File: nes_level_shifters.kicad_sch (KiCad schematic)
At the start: 17 parts, among them J2 NES 3v3 TP, U1 74ALVC164245, U2 74ALVC164245, U3 74ALVC164245, U4 74ALVC164245

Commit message: Create project-local libraries
Signed-off-by: Chris Frantz <frantzcj@gmail.com>
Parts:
- C10, C11, C12, C13, C14, C7, C8, C9: symbol Device:C -> Library:C
- J2: symbol Connector_Generic:Conn_02x36_Odd_Even -> Library:Conn_02x36_Odd_Even
- R43, R44, R45, R46: symbol Device:R -> Library:R
- U1, U2, U3, U4: symbol 74xx:74ALVC164245 -> Library:74ALVC164245
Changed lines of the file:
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@@
 	)
 	(symbol
-		(lib_id "Device:C")
+		(lib_id "Library:C")
 		(at 118.11 26.67 90)
 		(unit 1)
@@
 	)
 	(symbol
-		(lib_id "power:VCC")
+		(lib_id "Library:VCC")
 		(at 157.48 33.02 0)
 		(unit 1)
@@
 	)
 	(symbol
-		(lib_id "74xx:74ALVC164245")
+		(lib_id "Library:74ALVC164245")
 		(at 132.08 60.96 0)
 		(unit 1)
@@
 	)
 	(symbol
-		(lib_id "power:GND")
+		(lib_id "Library:GND")
 		(at 59.69 190.5 0)
 		(unit 1)
@@
 	)
 	(symbol
-		(lib_id "74xx:74ALVC164245")
+		(lib_id "Library:74ALVC164245")
 		(at 55.88 60.96 0)
 		(unit 1)
@@
 	)
 	(symbol
-		(lib_id "power:GND")
+		(lib_id "Library:GND")
 		(at 114.3 26.67 0)
 		(unit 1)
@@
 	)
 	(symbol
-		(lib_id "power:GND")
+		(lib_id "Library:GND")
 		(at 118.11 123.19 0)
 		(unit 1)
@@
 	)
 	(symbol
-		(lib_id "power:VCC")
+		(lib_id "Library:VCC")
 		(at 96.52 35.56 0)
 		(unit 1)
@@
 	)
 	(symbol
-		(lib_id "power:VCC")
+		(lib_id "Library:VCC")
 		(at 45.72 26.67 0)
 		(unit 1)
@@
 	)
 	(symbol
-		(lib_id "Device:R")
+		(lib_id "Library:R")
 		(at 96.52 39.37 0)
 		(unit 1)
@@
 	)
 	(symbol
-		(lib_id "Device:R")
+		(lib_id "Library:R")
 		(at 157.48 36.83 0)
 		(unit 1)
@@
 	)
 	(symbol
-		(lib_id "power:GND")
+		(lib_id "Library:GND")
 		(at 146.05 123.19 0)
 		(unit 1)
@@
 	)
 	(symbol
-		(lib_id "power:VCC")
+		(lib_id "Library:VCC")
 		(at 62.23 121.92 0)
 		(unit 1)
@@
 	)
 	(symbol
-		(lib_id "power:GND")
+		(lib_id "Library:GND")
 		(at 66.04 26.67 0)
 		(unit 1)
@@
 	)
 	(symbol
-		(lib_id "power:VCC")
+		(lib_id "Library:VCC")
 		(at 125.73 123.19 0)
 		(unit 1)
@@
 	)
 	(symbol
-		(lib_id "power:GND")
+		(lib_id "Library:GND")
 		(at 142.24 26.67 0)
 		(unit 1)
@@
 	)
 	(symbol
-		(lib_id "power:GND")
+		(lib_id "Library:GND")
 		(at 38.1 26.67 0)
 		(unit 1)
@@
 	)
 	(symbol
-		(lib_id "power:VCC")
+		(lib_id "Library:VCC")
 		(at 138.43 121.92 0)
 		(unit 1)
@@
 	)
 	(symbol
-		(lib_id "power:GND")
+		(lib_id "Library:GND")
 		(at 135.89 190.5 0)
 		(unit 1)
@@
 	)
 	(symbol
-		(lib_id "Device:C")
+		(lib_id "Library:C")
 		(at 41.91 26.67 90)
 		(unit 1)
@@
 	)
 	(symbol
-		(lib_id "power:VCC")
+		(lib_id "Library:VCC")
 		(at 49.53 123.19 0)
 		(unit 1)
@@
 	)
 	(symbol
-		(lib_id "Device:C")
+		(lib_id "Library:C")
 		(at 45.72 123.19 90)
 		(unit 1)
@@
 	)
 	(symbol
-		(lib_id "Device:C")
+		(lib_id "Library:C")
 		(at 138.43 26.67 90)
 		(unit 1)
@@
 	)
 	(symbol
-		(lib_id "power:VCC")
+		(lib_id "Library:VCC")
 		(at 58.42 22.86 0)
 		(unit 1)
@@
 	)
 	(symbol
-		(lib_id "power:GND")
+		(lib_id "Library:GND")
 		(at 69.85 123.19 0)
 		(unit 1)
@@
 	)
 	(symbol
-		(lib_id "power:VCC")
+		(lib_id "Library:VCC")
 		(at 38.1 132.08 0)
 		(unit 1)
@@
 	)
 	(symbol
-		(lib_id "power:GND")
+		(lib_id "Library:GND")
 		(at 41.91 123.19 0)
 		(unit 1)
@@
 	)
 	(symbol
-		(lib_id "Device:R")
+		(lib_id "Library:R")
 		(at 38.1 135.89 0)
 		(unit 1)
@@
 	)
 	(symbol
-		(lib_id "Device:C")
+		(lib_id "Library:C")
 		(at 66.04 123.19 90)
 		(unit 1)
@@
 	)
 	(symbol
-		(lib_id "Device:R")
+		(lib_id "Library:R")
 		(at 31.75 36.83 0)
 		(unit 1)
@@
 	)
 	(symbol
-		(lib_id "Connector_Generic:Conn_02x36_Odd_Even")
+		(lib_id "Library:Conn_02x36_Odd_Even")
 		(at 243.84 99.06 0)
 		(unit 1)
@@
 	)
 	(symbol
-		(lib_id "power:GND")
+		(lib_id "Library:GND")
 		(at 132.08 91.44 0)
 		(unit 1)
@@
 	)
 	(symbol
-		(lib_id "power:GND")
+		(lib_id "Library:GND")
 		(at 55.88 91.44 0)
 		(unit 1)
@@
 	)
 	(symbol
-		(lib_id "Device:C")
+		(lib_id "Library:C")
 		(at 62.23 26.67 90)
 		(unit 1)
@@
 	)
 	(symbol
-		(lib_id "74xx:74ALVC164245")
+		(lib_id "Library:74ALVC164245")
 		(at 135.89 160.02 0)
 		(unit 1)
@@
 	)
 	(symbol
-		(lib_id "Device:C")
+		(lib_id "Library:C")
 		(at 121.92 123.19 90)
 		(unit 1)
@@
 	)
 	(symbol
-		(lib_id "74xx:74ALVC164245")
+		(lib_id "Library:74ALVC164245")
 		(at 59.69 160.02 0)
 		(unit 1)
@@
 	)
 	(symbol
-		(lib_id "Device:C")
+		(lib_id "Library:C")
 		(at 142.24 123.19 90)
 		(unit 1)
@@
 	)
 	(symbol
-		(lib_id "power:GND")
+		(lib_id "Library:GND")
 		(at 105.41 142.24 0)
 		(unit 1)
@@
 	)
 	(symbol
-		(lib_id "power:VCC")
+		(lib_id "Library:VCC")
 		(at 121.92 26.67 0)
 		(unit 1)
@@
 	)
 	(symbol
-		(lib_id "power:VCC")
+		(lib_id "Library:VCC")
 		(at 134.62 22.86 0)
 		(unit 1)
@@
 	)
 	(symbol
-		(lib_id "power:VCC")
+		(lib_id "Library:VCC")
 		(at 31.75 33.02 0)
 		(unit 1)

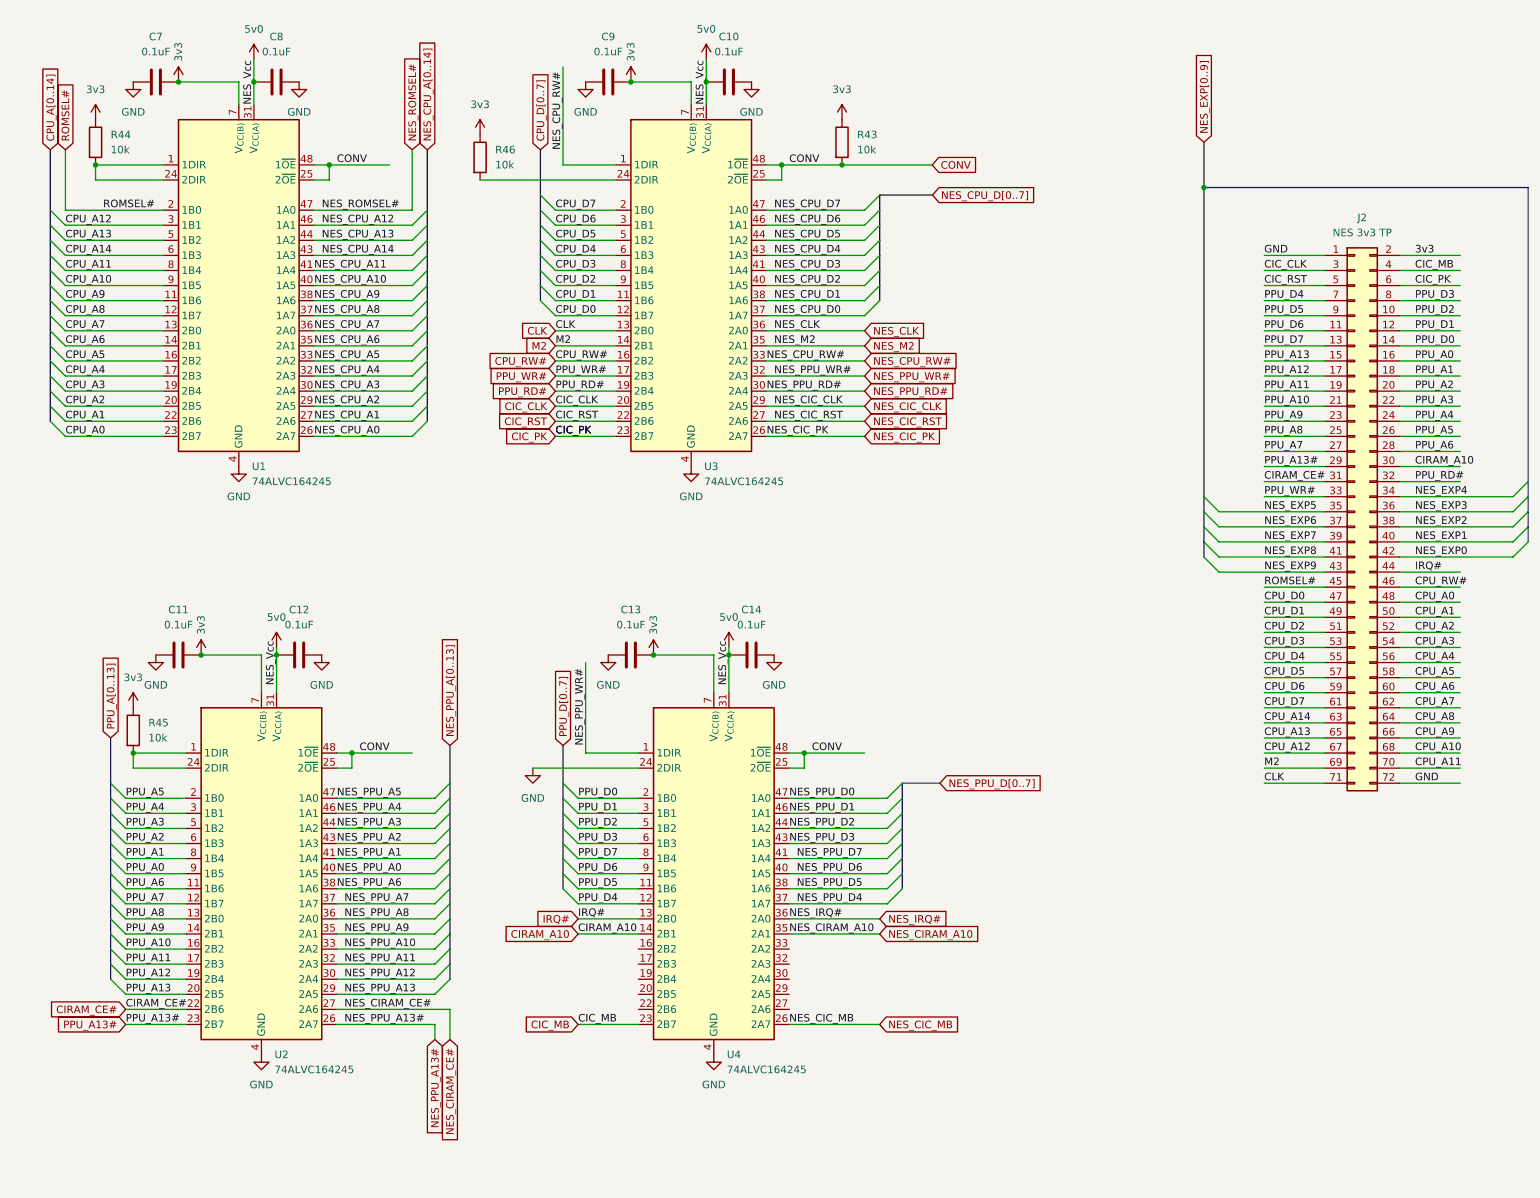
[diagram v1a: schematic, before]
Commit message: Update footprints and schematic.
1. Update teh HX8K eval board footprint to group power & grounds.
2. Re-arrange the level shifter section to try to get a better "straight
   through" layout.

Signed-off-by: Chris Frantz <frantzcj@gmail.com>
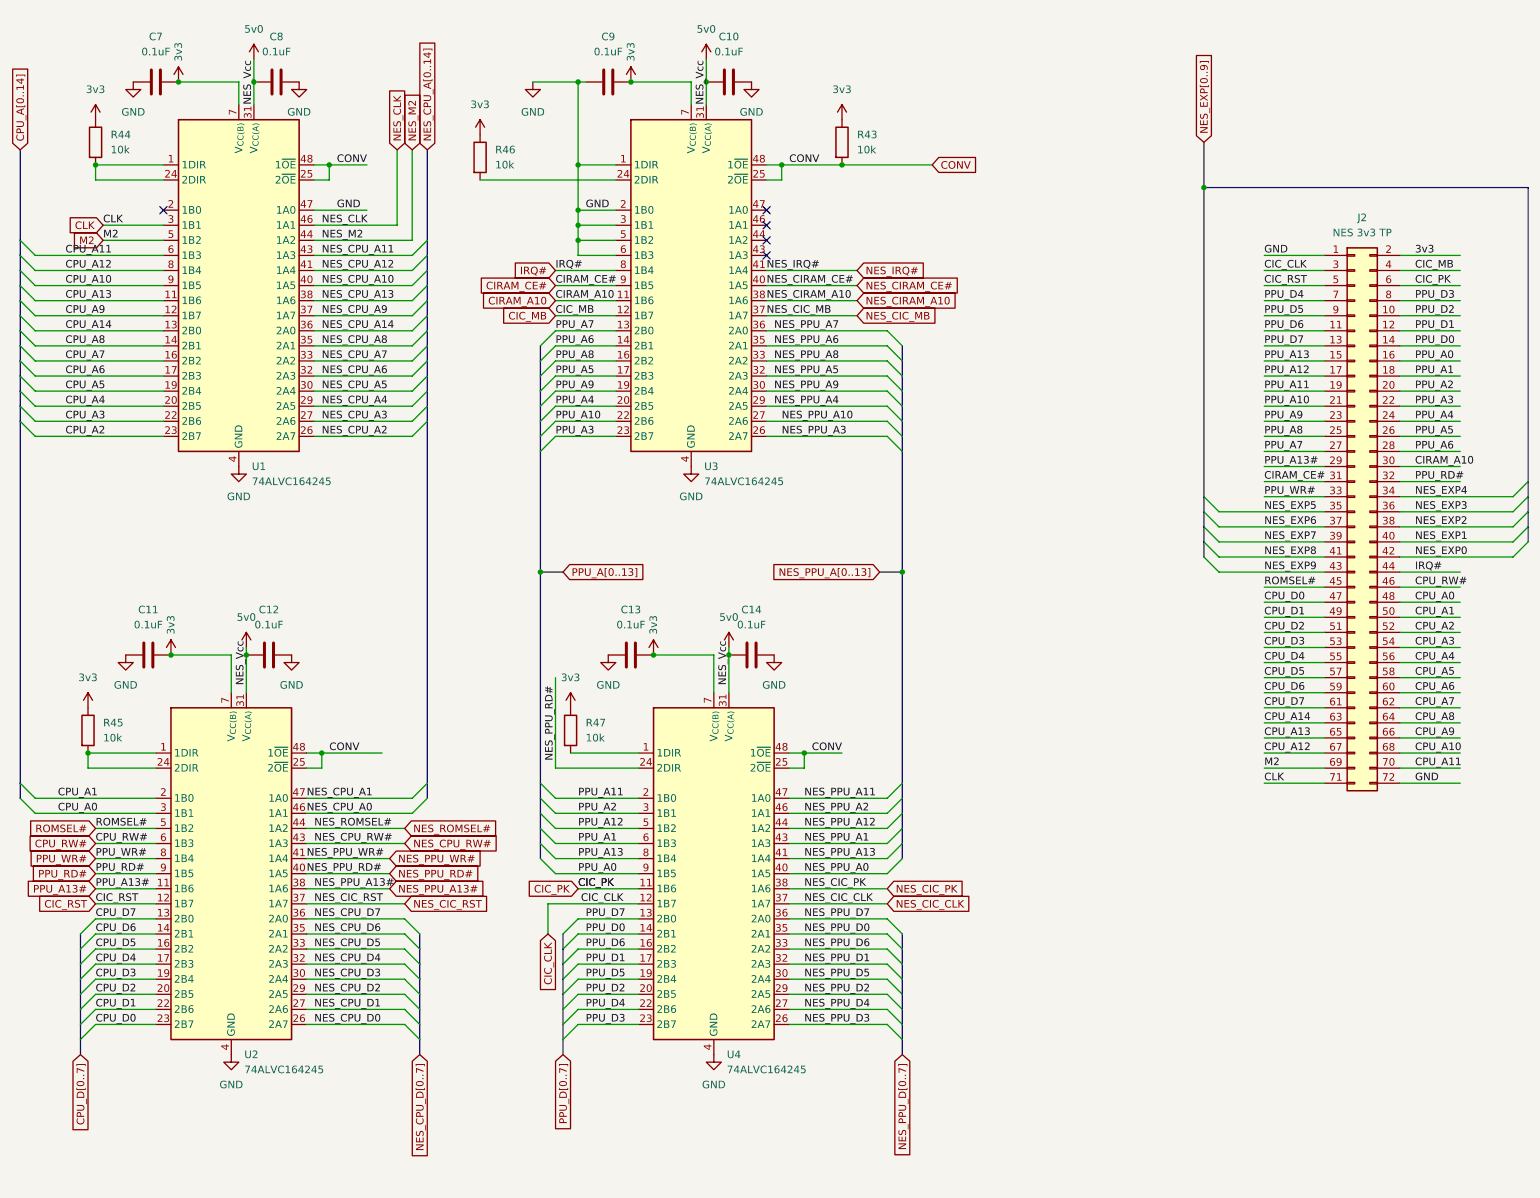
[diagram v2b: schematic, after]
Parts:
- added R47: 10k, Resistor_SMD:R_0402_1005Metric, symbol Library:R
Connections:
- net 3v3: now also R47.1
- net CIC_CLK: now also U4.12 (1B7); no longer U3.20 (2B5)
- net CIC_MB: now also U3.12 (1B7); no longer U4.23 (2B7)
- net CIC_PK: now also U4.11 (1B6); no longer U3.23 (2B7)
- net CIC_RST: now also U2.12 (1B7); no longer U3.22 (2B6)
- net CIRAM_A10: now also U3.11 (1B6); no longer U4.14 (2B1)
- net CIRAM_CE#: now also U3.9 (1B5); no longer U2.22 (2B6)
- net CLK: now also U1.3 (1B1); no longer U3.13 (2B0)
- net CPU_A0: now also U2.3 (1B1); no longer U1.23 (2B7)
- net CPU_A1: now also U2.2 (1B0); no longer U1.22 (2B6)
- net CPU_A11: now also U1.6 (1B3); no longer U1.8 (1B4)
- net CPU_A12: now also U1.8 (1B4); no longer U1.3 (1B1)
- net CPU_A13: now also U1.11 (1B6); no longer U1.5 (1B2)
- net CPU_A14: now also U1.13 (2B0); no longer U1.6 (1B3)
- net CPU_A2: now also U1.23 (2B7); no longer U1.20 (2B5)
- net CPU_A3: now also U1.22 (2B6); no longer U1.19 (2B4)
- net CPU_A4: now also U1.20 (2B5); no longer U1.17 (2B3)
- net CPU_A5: now also U1.19 (2B4); no longer U1.16 (2B2)
- net CPU_A6: now also U1.17 (2B3); no longer U1.14 (2B1)
- net CPU_A7: now also U1.16 (2B2); no longer U1.13 (2B0)
- net CPU_A8: now also U1.14 (2B1); no longer U1.12 (1B7)
- net CPU_A9: now also U1.12 (1B7); no longer U1.11 (1B6)
- net CPU_D0: now also U2.23 (2B7); no longer U3.12 (1B7)
- net CPU_D1: now also U2.22 (2B6); no longer U3.11 (1B6)
- net CPU_D2: now also U2.20 (2B5); no longer U3.9 (1B5)
- net CPU_D3: now also U2.19 (2B4); no longer U3.8 (1B4)
- net CPU_D4: now also U2.17 (2B3); no longer U3.6 (1B3)
- net CPU_D5: now also U2.16 (2B2); no longer U3.5 (1B2)
- net CPU_D6: now also U2.14 (2B1); no longer U3.3 (1B1)
- net CPU_D7: now also U2.13 (2B0); no longer U3.2 (1B0)
- net CPU_RW#: now also U2.6 (1B3); no longer U3.16 (2B2)
- net GND: now also U1.47 (1A0), U3.1 (1DIR), U3.2 (1B0), U3.3 (1B1), U3.5 (1B2), U3.6 (1B3); no longer U4.24 (2DIR)
- net IRQ#: now also U3.8 (1B4); no longer U4.13 (2B0)
- net M2: now also U1.5 (1B2); no longer U3.14 (2B1)
- net NES_CIC_CLK: now also U4.37 (1A7); no longer U3.29 (2A5)
- net NES_CIC_MB: now also U3.37 (1A7); no longer U4.26 (2A7)
- net NES_CIC_PK: now also U4.38 (1A6); no longer U3.26 (2A7)
- net NES_CIC_RST: now also U2.37 (1A7); no longer U3.27 (2A6)
- net NES_CIRAM_A10: now also U3.38 (1A6); no longer U4.35 (2A1)
- net NES_CIRAM_CE#: now also U3.40 (1A5); no longer U2.27 (2A6)
- net NES_CLK: now also U1.46 (1A1); no longer U3.36 (2A0)
- net NES_CPU_A0: now also U2.46 (1A1); no longer U1.26 (2A7)
- net NES_CPU_A1: now also U2.47 (1A0); no longer U1.27 (2A6)
- net NES_CPU_A11: now also U1.43 (1A3); no longer U1.41 (1A4)
- net NES_CPU_A12: now also U1.41 (1A4); no longer U1.46 (1A1)
- net NES_CPU_A13: now also U1.38 (1A6); no longer U1.44 (1A2)
- net NES_CPU_A14: now also U1.36 (2A0); no longer U1.43 (1A3)
- net NES_CPU_A2: now also U1.26 (2A7); no longer U1.29 (2A5)
- net NES_CPU_A3: now also U1.27 (2A6); no longer U1.30 (2A4)
- net NES_CPU_A4: now also U1.29 (2A5); no longer U1.32 (2A3)
- net NES_CPU_A5: now also U1.30 (2A4); no longer U1.33 (2A2)
- net NES_CPU_A6: now also U1.32 (2A3); no longer U1.35 (2A1)
- net NES_CPU_A7: now also U1.33 (2A2); no longer U1.36 (2A0)
- net NES_CPU_A8: now also U1.35 (2A1); no longer U1.37 (1A7)
- net NES_CPU_A9: now also U1.37 (1A7); no longer U1.38 (1A6)
- net NES_CPU_D0: now also U2.26 (2A7); no longer U3.37 (1A7)
- net NES_CPU_D1: now also U2.27 (2A6); no longer U3.38 (1A6)
- net NES_CPU_D2: now also U2.29 (2A5); no longer U3.40 (1A5)
- net NES_CPU_D3: now also U2.30 (2A4); no longer U3.41 (1A4)
- net NES_CPU_D4: now also U2.32 (2A3); no longer U3.43 (1A3)
- net NES_CPU_D5: now also U2.33 (2A2); no longer U3.44 (1A2)
- net NES_CPU_D6: now also U2.35 (2A1); no longer U3.46 (1A1)
- net NES_CPU_D7: now also U2.36 (2A0); no longer U3.47 (1A0)
- net NES_CPU_RW#: now also U2.43 (1A3); no longer U3.1 (1DIR), U3.33 (2A2)
- net NES_IRQ#: now also U3.41 (1A4); no longer U4.36 (2A0)
- net NES_M2: now also U1.44 (1A2); no longer U3.35 (2A1)
- net NES_PPU_A0: now also U4.40 (1A5); no longer U2.40 (1A5)
- net NES_PPU_A1: now also U4.43 (1A3); no longer U2.41 (1A4)
- net NES_PPU_A10: now also U3.27 (2A6); no longer U2.33 (2A2)
- net NES_PPU_A11: now also U4.47 (1A0); no longer U2.32 (2A3)
- net NES_PPU_A12: now also U4.44 (1A2); no longer U2.30 (2A4)
- net NES_PPU_A13: now also U4.41 (1A4); no longer U2.29 (2A5)
- net NES_PPU_A13#: now also U2.38 (1A6); no longer U2.26 (2A7)
- net NES_PPU_A2: now also U4.46 (1A1); no longer U2.43 (1A3)
- net NES_PPU_A3: now also U3.26 (2A7); no longer U2.44 (1A2)
- net NES_PPU_A4: now also U3.29 (2A5); no longer U2.46 (1A1)
- net NES_PPU_A5: now also U3.32 (2A3); no longer U2.47 (1A0)
- net NES_PPU_A6: now also U3.35 (2A1); no longer U2.38 (1A6)
- net NES_PPU_A7: now also U3.36 (2A0); no longer U2.37 (1A7)
- net NES_PPU_A8: now also U3.33 (2A2); no longer U2.36 (2A0)
- net NES_PPU_A9: now also U3.30 (2A4); no longer U2.35 (2A1)
- net NES_PPU_D0: now also U4.35 (2A1); no longer U4.47 (1A0)
- net NES_PPU_D1: now also U4.32 (2A3); no longer U4.46 (1A1)
- net NES_PPU_D2: now also U4.29 (2A5); no longer U4.44 (1A2)
- net NES_PPU_D3: now also U4.26 (2A7); no longer U4.43 (1A3)
- net NES_PPU_D4: now also U4.27 (2A6); no longer U4.37 (1A7)
- net NES_PPU_D5: now also U4.30 (2A4); no longer U4.38 (1A6)
- net NES_PPU_D6: now also U4.33 (2A2); no longer U4.40 (1A5)
- net NES_PPU_D7: now also U4.36 (2A0); no longer U4.41 (1A4)
- net NES_PPU_RD#: now also U2.40 (1A5), U4.24 (2DIR); no longer U3.30 (2A4)
- net NES_PPU_WR#: now also U2.41 (1A4); no longer U3.32 (2A3), U4.1 (1DIR)
- net NES_ROMSEL#: now also U2.44 (1A2); no longer U1.47 (1A0)
- net PPU_A0: now also U4.9 (1B5); no longer U2.9 (1B5)
- net PPU_A1: now also U4.6 (1B3); no longer U2.8 (1B4)
- net PPU_A10: now also U3.22 (2B6); no longer U2.16 (2B2)
- net PPU_A11: now also U4.2 (1B0); no longer U2.17 (2B3)
- net PPU_A12: now also U4.5 (1B2); no longer U2.19 (2B4)
- net PPU_A13: now also U4.8 (1B4); no longer U2.20 (2B5)
- net PPU_A13#: now also U2.11 (1B6); no longer U2.23 (2B7)
- net PPU_A2: now also U4.3 (1B1); no longer U2.6 (1B3)
- net PPU_A3: now also U3.23 (2B7); no longer U2.5 (1B2)
- net PPU_A4: now also U3.20 (2B5); no longer U2.3 (1B1)
- net PPU_A5: now also U3.17 (2B3); no longer U2.2 (1B0)
- net PPU_A6: now also U3.14 (2B1); no longer U2.11 (1B6)
- net PPU_A7: now also U3.13 (2B0); no longer U2.12 (1B7)
- net PPU_A8: now also U3.16 (2B2); no longer U2.13 (2B0)
- net PPU_A9: now also U3.19 (2B4); no longer U2.14 (2B1)
- net PPU_D0: now also U4.14 (2B1); no longer U4.2 (1B0)
- net PPU_D1: now also U4.17 (2B3); no longer U4.3 (1B1)
- net PPU_D2: now also U4.20 (2B5); no longer U4.5 (1B2)
- net PPU_D3: now also U4.23 (2B7); no longer U4.6 (1B3)
- net PPU_D4: now also U4.22 (2B6); no longer U4.12 (1B7)
- net PPU_D5: now also U4.19 (2B4); no longer U4.11 (1B6)
- net PPU_D6: now also U4.16 (2B2); no longer U4.9 (1B5)
- net PPU_D7: now also U4.13 (2B0); no longer U4.8 (1B4)
- net PPU_RD#: now also U2.9 (1B5); no longer U3.19 (2B4)
- net PPU_WR#: now also U2.8 (1B4); no longer U3.17 (2B3)
- net ROMSEL#: now also U2.5 (1B2); no longer U1.2 (1B0)
- new net: R47.2, U4.1 (1DIR)
- no-connect marks 0 -> 5
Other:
- moved on the sheet: C11, C12, U2
